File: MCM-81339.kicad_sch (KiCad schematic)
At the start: 4 parts

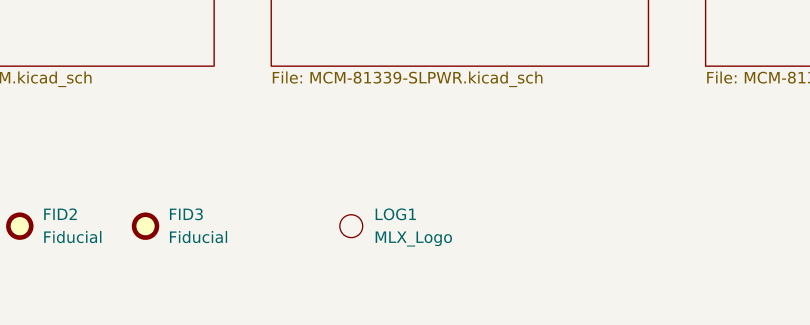
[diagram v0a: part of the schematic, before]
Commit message: add protection on uart, add fab outputs
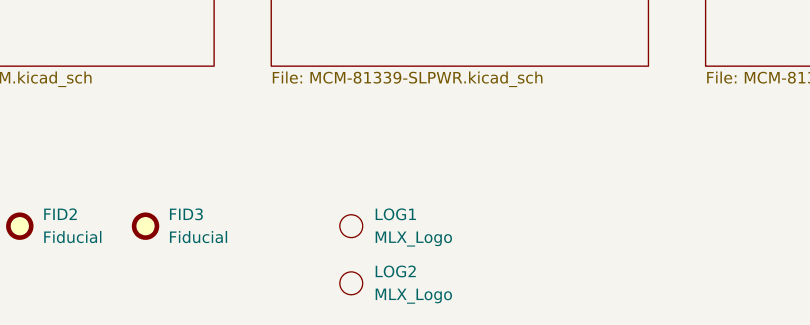
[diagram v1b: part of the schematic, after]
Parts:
- added LOG2: MLX_Logo, Melexis:LOGO, symbol Melexis:MLX_Logo
- LOG1: footprint Melexis:LOGO -> Melexis:LOGO-SILK
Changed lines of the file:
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@@
+    )
+  )
+  (symbol (lib_id "Melexis:MLX_Logo") (at 161.29 127 0) (unit 1)
+    (in_bom yes) (on_board yes) (fields_autoplaced)
+    (property "Reference" "LOG2" (id 0) (at 163.83 125.7299 0)
+      (effects (font (size 1.27 1.27)) (justify left))
+    )
+    (property "Value" "MLX_Logo" (id 1) (at 163.83 128.2699 0)
+      (effects (font (size 1.27 1.27)) (justify left))
+    )
+    (property "Footprint" "Melexis:LOGO" (id 2) (at 161.29 127 0)
+      (effects (font (size 1.27 1.27)) hide)
+    )
+    (property "Datasheet" "" (id 3) (at 161.29 127 0)
+      (effects (font (size 1.27 1.27)) hide)
     )
   )
@@
       (effects (font (size 1.27 1.27)) (justify left))
     )
-    (property "Footprint" "Melexis:LOGO" (id 2) (at 161.29 120.65 0)
+    (property "Footprint" "Melexis:LOGO-SILK" (id 2) (at 161.29 120.65 0)
       (effects (font (size 1.27 1.27)) hide)
     )
@@
       (reference "#PWR01") (unit 1) (value "GND") (footprint "")
     )
+    (path "/9c2d2be5-5ec8-4be4-ace1-11635aa4e179/8f2aa309-a9c1-4073-9637-445c5bf7b2da"
+      (reference "#PWR02") (unit 1) (value "GND") (footprint "")
+    )
+    (path "/9c2d2be5-5ec8-4be4-ace1-11635aa4e179/32ca398c-f7bd-46c0-9737-cffb8bb255c0"
+      (reference "#PWR03") (unit 1) (value "GND") (footprint "")
+    )
     (path "/9c2d2be5-5ec8-4be4-ace1-11635aa4e179/09421454-0739-461d-aa48-dd17b4242db4"
       (reference "#PWR0101") (unit 1) (value "GND") (footprint "")
@@
     )
     (path "/72c7d519-8696-4dcf-8164-31de870ed890/25c4749a-6b5d-40ec-9530-48e5db6b92e5"
-      (reference "D1") (unit 1) (value "LED") (footprint "LED_SMD:LED_0603_1608Metric")
+      (reference "D1") (unit 1) (value "150060RS55040") (footprint "LED_SMD:LED_0603_1608Metric")
     )
     (path "/72c7d519-8696-4dcf-8164-31de870ed890/f26d3d5c-9c24-47e7-9992-09f2fea7c43c"
@@
     )
     (path "/21b6716c-4e9d-4023-be1b-784c50e050b4/7475933b-d843-4b83-9338-d896f8c1b05f"
-      (reference "D6") (unit 1) (value "LED") (footprint "LED_SMD:LED_0603_1608Metric")
+      (reference "D6") (unit 1) (value "150060VS55040") (footprint "LED_SMD:LED_0603_1608Metric")
     )
     (path "/d7f02b87-6965-431a-ae0a-8f71dbafb872/2e5d5d6d-66e5-480c-9d70-d3c142363262"
-      (reference "D7") (unit 1) (value "LED") (footprint "LED_SMD:LED_0603_1608Metric")
+      (reference "D7") (unit 1) (value "150060VS55040") (footprint "LED_SMD:LED_0603_1608Metric")
     )
     (path "/d7f02b87-6965-431a-ae0a-8f71dbafb872/8345625a-2806-457d-89f5-d8c4b2c12e0f"
@@
     )
     (path "/d7f02b87-6965-431a-ae0a-8f71dbafb872/42fff36f-bacf-4bdf-a68a-1203b70d1064"
-      (reference "D10") (unit 1) (value "LED") (footprint "LED_SMD:LED_0603_1608Metric")
+      (reference "D10") (unit 1) (value "150060RS55040") (footprint "LED_SMD:LED_0603_1608Metric")
     )
     (path "/d7f02b87-6965-431a-ae0a-8f71dbafb872/990b8ae3-c48c-4659-a142-5c4eb282fb7e"
@@
       (reference "D17") (unit 1) (value "D20V0L1B2WS-7") (footprint "Diode_SMD:D_SOD-323")
     )
+    (path "/9c2d2be5-5ec8-4be4-ace1-11635aa4e179/6acdedc3-7ccb-406d-be1f-12a681904294"
+      (reference "D18") (unit 1) (value "ESD9B5.0ST5G") (footprint "Diode_SMD:D_SOD-923")
+    )
+    (path "/9c2d2be5-5ec8-4be4-ace1-11635aa4e179/61850d8d-9fa9-4f22-8dca-7e9504ab3edc"
+      (reference "D19") (unit 1) (value "ESD9B5.0ST5G") (footprint "Diode_SMD:D_SOD-923")
+    )
     (path "/93880ec1-d1c9-4359-b0f2-607a8c3df269"
       (reference "FID1") (unit 1) (value "Fiducial") (footprint "Fiducial:Fiducial_0.5mm_Mask1mm")
@@
     )
     (path "/edcd3dbc-bcef-43b5-9116-9ff8527310ce"
-      (reference "LOG1") (unit 1) (value "MLX_Logo") (footprint "Melexis:LOGO")
+      (reference "LOG1") (unit 1) (value "MLX_Logo") (footprint "Melexis:LOGO-SILK")
+    )
+    (path "/18df3d8d-86e5-4aab-b378-ffaba5fbd037"
+      (reference "LOG2") (unit 1) (value "MLX_Logo") (footprint "Melexis:LOGO")
     )
     (path "/72c7d519-8696-4dcf-8164-31de870ed890/9b474d04-fde8-43e1-be6e-3173d40c13ec"
@@
       (reference "R14") (unit 1) (value "2k") (footprint "Resistor_SMD:R_0603_1608Metric")
     )
+    (path "/9c2d2be5-5ec8-4be4-ace1-11635aa4e179/faa2685a-fd96-4c96-bedb-a89159f56d6b"
+      (reference "R15") (unit 1) (value "100R") (footprint "Resistor_SMD:R_0402_1005Metric")
+    )
+    (path "/9c2d2be5-5ec8-4be4-ace1-11635aa4e179/2b5e7d81-c273-4960-af76-3378bc4ef8f6"
+      (reference "R16") (unit 1) (value "100R") (footprint "Resistor_SMD:R_0402_1005Metric")
+    )
     (path "/d7f02b87-6965-431a-ae0a-8f71dbafb872/87df298f-1c8a-49b1-b11f-75bd3967a21b"
       (reference "R17") (unit 1) (value "2k") (footprint "Resistor_SMD:R_0603_1608Metric")
@@
       (reference "R27") (unit 1) (value "100k") (footprint "Resistor_SMD:R_0402_1005Metric")
     )
+    (path "/9c2d2be5-5ec8-4be4-ace1-11635aa4e179/18ab717b-c619-44b7-a60e-cd65e722150f"
+      (reference "R28") (unit 1) (value "100R") (footprint "Resistor_SMD:R_0402_1005Metric")
+    )
     (path "/9c2d2be5-5ec8-4be4-ace1-11635aa4e179/b74e1651-bf5b-48b7-b6de-a896822e5efa"
       (reference "R29") (unit 1) (value "0R") (footprint "Resistor_SMD:R_0603_1608Metric")
     )
+    (path "/9c2d2be5-5ec8-4be4-ace1-11635aa4e179/400b3133-5c30-4ed4-9a3b-7eb45c7a9123"
+      (reference "R30") (unit 1) (value "100R") (footprint "Resistor_SMD:R_0402_1005Metric")
+    )
     (path "/9c2d2be5-5ec8-4be4-ace1-11635aa4e179/e96d393c-81a3-4a8e-9c0c-5ff131b5939e"
